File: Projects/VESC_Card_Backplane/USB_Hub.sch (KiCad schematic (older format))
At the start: 22 parts

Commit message: Added stuff to VESC_Card_Backplane
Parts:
- removed USB? (x3): USB-TYPA, USB-A-F-PTH, symbol USB-TYPA
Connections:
- net labels added: DM_1, DM_2, DM_3, DP_1, DP_2, DP_3
- wire segments 94 -> 87
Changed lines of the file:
@@
-	1    0    0    -1
-$EndComp
-$Comp
-L +5V #U$07
-U 1 1 57E6D8D3
-P 8450 6350
-F 0 "#U$07" H 8375 6450 60  0001 L BNN
-F 1 "+5V" H 8350 6500 60  0000 L BNN
-F 2 "" H 8450 6350 60  0001 C CNN
-F 3 "" H 8450 6350 60  0001 C CNN
-	1    8450 6350
 	1    0    0    -1
 $EndComp
@@
 GND
 Text GLabel 4650 6800 3    10   UnSpc ~ 0
-GND
-Text GLabel 6650 5550 3    10   UnSpc ~ 0
-GND
-Text GLabel 6650 6950 1    10   UnSpc ~ 0
-GND
-Text GLabel 7050 5850 3    10   UnSpc ~ 0
-GND
-Text GLabel 7450 6150 3    10   UnSpc ~ 0
 GND
 Text Label 4750 5850 0    10   ~ 0
@@
 Text Label 4600 4750 0    10   ~ 0
 VBUS
-Text Label 6950 5550 3    10   ~ 0
-VBUS
-Text Label 7750 6150 3    10   ~ 0
-VBUS
 Text Label 7350 5850 3    10   ~ 0
-VBUS
-Text Label 8450 6350 3    10   ~ 0
 VBUS
 $Comp
@@
 $EndComp
 $Comp
-L USB-TYPA USB?
-U 1 1 58632E73
-P 7600 5900
-F 0 "USB?" H 7600 6150 45  0000 C CNN
-F 1 "USB-TYPA" V 7700 5900 45  0000 C CNN
-F 2 "USB-A-F-PTH" H 7600 5600 20  0001 C CNN
-F 3 "" H 7600 5900 60  0000 C CNN
-	1    7600 5900
-	0    1    -1   0
-$EndComp
-$Comp
-L USB-TYPA USB?
-U 1 1 586331D9
-P 6800 5300
-F 0 "USB?" H 6800 5550 45  0000 C CNN
-F 1 "USB-TYPA" V 6900 5300 45  0000 C CNN
-F 2 "USB-A-F-PTH" H 6800 5000 20  0001 C CNN
-F 3 "" H 6800 5300 60  0000 C CNN
-	1    6800 5300
-	0    1    -1   0
-$EndComp
-$Comp
-L USB-TYPA USB?
-U 1 1 58633244
-P 7200 5600
-F 0 "USB?" H 7200 5850 45  0000 C CNN
-F 1 "USB-TYPA" V 7300 5600 45  0000 C CNN
-F 2 "USB-A-F-PTH" H 7200 5300 20  0001 C CNN
-F 3 "" H 7200 5600 60  0000 C CNN
-	1    7200 5600
-	0    1    -1   0
-$EndComp
-$Comp
 L XTAL_1 XL1
 U 1 1 57E6DDE7
@@
 	0    1    -1   0
 $EndComp
-$Comp
-L GND #GND?
-U 1 1 586383BE
-P 6650 6950
-F 0 "#GND?" H 6650 6950 45  0001 L BNN
-F 1 "GND" H 6600 6775 45  0000 L BNN
-F 2 "" H 6650 6950 60  0001 C CNN
-F 3 "" H 6650 6950 60  0001 C CNN
-	1    6650 6950
+Text HLabel 4850 7600 0    60   Input ~ 0
+DM_U
+Text HLabel 4850 7700 0    60   Input ~ 0
+DP_U
+Text Notes 4900 7850 0    60   ~ 0
+Upstream USB Connection
+$Comp
+L VDD #PWR?
+U 1 1 58718D88
+P 4850 5350
+F 0 "#PWR?" H 4850 5200 50  0001 C CNN
+F 1 "VDD" H 4850 5500 50  0000 C CNN
+F 2 "" H 4850 5350 50  0000 C CNN
+F 3 "" H 4850 5350 50  0000 C CNN
+	1    4850 5350
 	1    0    0    -1
 $EndComp
+Text HLabel 8050 6450 1    60   Input ~ 0
+DM_4
+Text HLabel 7950 6450 1    60   Input ~ 0
+DP_4
+Text HLabel 7650 6150 1    60   Input ~ 0
+DM_3
+Text HLabel 7550 6150 1    60   Input ~ 0
+DP_3
+Text HLabel 7250 5850 1    60   Input ~ 0
+DM_2
+Text HLabel 7150 5850 1    60   Input ~ 0
+DP_2
+Text HLabel 6850 5550 1    60   Input ~ 0
+DM_1
+Text HLabel 6750 5550 1    60   Input ~ 0
+DP_1
+$Comp
+L GND #PWR?
+U 1 1 5871A6C2
+P 2250 6775
+F 0 "#PWR?" H 2250 6525 50  0001 C CNN
+F 1 "GND" H 2250 6625 50  0000 C CNN
+F 2 "" H 2250 6775 50  0000 C CNN
+F 3 "" H 2250 6775 50  0000 C CNN
+	1    2250 6775
+	1    0    0    -1
+$EndComp
+$Comp
+L +5V #PWR?
+U 1 1 5871A6FC
+P 2175 5325
+F 0 "#PWR?" H 2175 5175 50  0001 C CNN
+F 1 "+5V" H 2175 5465 50  0000 C CNN
+F 2 "" H 2175 5325 50  0000 C CNN
+F 3 "" H 2175 5325 50  0000 C CNN
+	1    2175 5325
+	1    0    0    -1
+$EndComp
+Text HLabel 2250 6575 1    60   Input ~ 0
+GND
+Text HLabel 2175 5600 3    60   Input ~ 0
++5V
 Wire Wire Line
 	5300 5150 5250 5150
@@
 Wire Wire Line
 	4850 6350 5300 6350
-Wire Wire Line
-	5250 6350 5250 6250
 Wire Wire Line
 	4850 6350 4850 6450
@@
 Connection ~ 4650 6850
 Wire Wire Line
-	6650 5550 6650 6950
-Wire Wire Line
-	7050 5850 7050 6850
-Wire Wire Line
-	7450 6850 7450 6150
-Connection ~ 6650 6850
-Connection ~ 7050 6850
-Connection ~ 7450 6850
-Wire Wire Line
-	7650 5350 7650 5250
+	7650 5200 7650 5350
 Wire Wire Line
 	4700 5850 5300 5850
@@
 Connection ~ 4700 4750
 Wire Wire Line
-	6950 5550 6950 6750
-Wire Wire Line
-	7750 6750 7750 6150
-Wire Wire Line
-	6950 6750 8450 6750
-Wire Wire Line
-	7350 5850 7350 6750
-Wire Wire Line
-	8450 6750 8450 6350
-Connection ~ 7750 6750
-Connection ~ 7350 6750
-Text HLabel 4850 7600 0    60   Input ~ 0
-DM_U
-Text HLabel 4850 7700 0    60   Input ~ 0
-DP_U
-Text Notes 4900 7850 0    60   ~ 0
-Upstream USB Connection
-$Comp
-L VDD #PWR?
-U 1 1 58718D88
-P 4850 5350
-F 0 "#PWR?" H 4850 5200 50  0001 C CNN
-F 1 "VDD" H 4850 5500 50  0000 C CNN
-F 2 "" H 4850 5350 50  0000 C CNN
-F 3 "" H 4850 5350 50  0000 C CNN
-	1    4850 5350
-	1    0    0    -1
-$EndComp
-Text HLabel 8050 6450 1    60   Input ~ 0
-DM_4
-Text HLabel 7950 6450 1    60   Input ~ 0
-DP_4
-Wire Wire Line
-	6650 6850 7450 6850
+	5250 6350 5250 6250
+Wire Wire Line
+	2175 5325 2175 5600
+Wire Wire Line
+	2250 6575 2250 6775
 $EndSCHEMATC

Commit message: Updated subsheets and added CAN bus :)
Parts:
- added JP1: Jumper_NC_Small, symbol Jumper_NC_Small
- added U1: LP38693, symbol LP38693
- gave numbers to parts that had none: 1
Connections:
- net labels added: GNDD
- wire segments 87 -> 94
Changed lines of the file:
@@
 $Descr A3 16535 11693
 encoding utf-8
-Sheet 2 5
+Sheet 2 6
 Title "RH025.1.sch"
 Date "24 SEP 2016"
@@
 $EndComp
 $Comp
-L GND #GND03
+L GNDD #GND1
 U 1 1 57E6CBEF
 P 4550 6900
-F 0 "#GND03" H 4450 6900 60  0001 L BNN
-F 1 "GND" H 4475 6725 60  0000 L BNN
+F 0 "#GND1" H 4450 6900 60  0001 L BNN
+F 1 "GNDD" H 4475 6725 60  0000 L BNN
 F 2 "" H 4550 6900 60  0001 C CNN
 F 3 "" H 4550 6900 60  0001 C CNN
@@
 $EndComp
 $Comp
-L GND #GND04
+L GNDD #GND2
 U 1 1 57E6CC53
 P 7650 5350
-F 0 "#GND04" H 7550 5350 60  0001 L BNN
-F 1 "GND" H 7575 5175 60  0000 L BNN
+F 0 "#GND2" H 7550 5350 60  0001 L BNN
+F 1 "GNDD" H 7575 5175 60  0000 L BNN
 F 2 "" H 7650 5350 60  0001 C CNN
 F 3 "" H 7650 5350 60  0001 C CNN
@@
 $EndComp
 $Comp
-L +5V #U$05
+L +5V #U$2
 U 1 1 57E6D80B
 P 5250 4300
-F 0 "#U$05" H 5175 4400 60  0001 L BNN
+F 0 "#U$2" H 5175 4400 60  0001 L BNN
 F 1 "+5V" H 5150 4500 60  0000 L BNN
 F 2 "" H 5250 4300 60  0001 C CNN
@@
 VBUS
 $Comp
-L FE1.1S M?
+L FE1.1S M1
 U 1 1 5862FDC9
 P 5900 5550
-F 0 "M?" H 5500 6780 45  0000 L BNN
+F 0 "M1" H 5500 6780 45  0000 L BNN
 F 1 "FE1.1S" H 5900 5550 45  0001 L BNN
 F 2 "FE1.1S_SSOP-28" H 5930 5700 20  0001 C CNN
@@
 Upstream USB Connection
 $Comp
-L VDD #PWR?
+L VDD #PWR2
 U 1 1 58718D88
 P 4850 5350
-F 0 "#PWR?" H 4850 5200 50  0001 C CNN
+F 0 "#PWR2" H 4850 5200 50  0001 C CNN
 F 1 "VDD" H 4850 5500 50  0000 C CNN
 F 2 "" H 4850 5350 50  0000 C CNN
@@
 DP_1
 $Comp
-L GND #PWR?
+L GNDD #PWR1
 U 1 1 5871A6C2
-P 2250 6775
-F 0 "#PWR?" H 2250 6525 50  0001 C CNN
-F 1 "GND" H 2250 6625 50  0000 C CNN
-F 2 "" H 2250 6775 50  0000 C CNN
-F 3 "" H 2250 6775 50  0000 C CNN
-	1    2250 6775
-	1    0    0    -1
-$EndComp
-$Comp
-L +5V #PWR?
-U 1 1 5871A6FC
-P 2175 5325
-F 0 "#PWR?" H 2175 5175 50  0001 C CNN
-F 1 "+5V" H 2175 5465 50  0000 C CNN
-F 2 "" H 2175 5325 50  0000 C CNN
-F 3 "" H 2175 5325 50  0000 C CNN
-	1    2175 5325
-	1    0    0    -1
-$EndComp
-Text HLabel 2250 6575 1    60   Input ~ 0
-GND
-Text HLabel 2175 5600 3    60   Input ~ 0
+P 3350 6375
+F 0 "#PWR1" H 3350 6125 50  0001 C CNN
+F 1 "GNDD" H 3350 6225 50  0000 C CNN
+F 2 "" H 3350 6375 50  0000 C CNN
+F 3 "" H 3350 6375 50  0000 C CNN
+	1    3350 6375
+	1    0    0    -1
+$EndComp
+Text HLabel 3350 6175 1    60   Input ~ 0
+GND
+Text HLabel 3350 5600 3    60   Input ~ 0
 +5V
 Wire Wire Line
@@
 	5200 6550 5300 6550
 Wire Wire Line
-	4850 6750 4850 6850
-Wire Wire Line
-	4850 6850 4100 6850
+	4850 6850 4850 6750
+Wire Wire Line
+	4100 6850 4850 6850
 Wire Wire Line
 	4550 6850 4550 6900
@@
 	4100 5850 4400 5850
 Wire Wire Line
-	4100 6850 4100 4450
+	4100 4450 4100 6850
 Wire Wire Line
 	4100 4450 5300 4450
@@
 	5250 6350 5250 6250
 Wire Wire Line
-	2175 5325 2175 5600
-Wire Wire Line
-	2250 6575 2250 6775
+	3350 6175 3350 6375
+Wire Wire Line
+	3350 5600 3350 5350
+$Comp
+L +5V #U$1
+U 1 1 587820C5
+P 3350 5350
+F 0 "#U$1" H 3275 5450 60  0001 L BNN
+F 1 "+5V" H 3250 5550 60  0000 L BNN
+F 2 "" H 3350 5350 60  0001 C CNN
+F 3 "" H 3350 5350 60  0001 C CNN
+	1    3350 5350
+	1    0    0    -1
+$EndComp
+$Comp
+L LP38693 U1
+U 1 1 58783463
+P 10100 5400
+F 0 "U1" H 10250 5100 60  0000 C CNN
+F 1 "LP38693" H 10100 5700 60  0000 C CNN
+F 2 "" H 10100 5400 60  0001 C CNN
+F 3 "" H 10100 5400 60  0001 C CNN
+	1    10100 5400
+	1    0    0    -1
+$EndComp
+$Comp
+L VDD #PWR3
+U 1 1 587837CA
+P 10900 5350
+F 0 "#PWR3" H 10900 5200 50  0001 C CNN
+F 1 "VDD" H 10900 5500 50  0000 C CNN
+F 2 "" H 10900 5350 50  0000 C CNN
+F 3 "" H 10900 5350 50  0000 C CNN
+	1    10900 5350
+	1    0    0    -1
+$EndComp
+Wire Wire Line
+	10900 5350 10900 5400
+Wire Wire Line
+	10900 5400 10550 5400
+Wire Wire Line
+	9650 5400 9150 5400
+Wire Wire Line
+	9150 5400 9150 5350
+$Comp
+L +5V #U$3
+U 1 1 58783B06
+P 9150 5350
+F 0 "#U$3" H 9075 5450 60  0001 L BNN
+F 1 "+5V" H 9050 5550 60  0000 L BNN
+F 2 "" H 9150 5350 60  0001 C CNN
+F 3 "" H 9150 5350 60  0001 C CNN
+	1    9150 5350
+	1    0    0    -1
+$EndComp
+$Comp
+L GNDD #GND3
+U 1 1 58784370
+P 10100 5900
+F 0 "#GND3" H 10000 5900 60  0001 L BNN
+F 1 "GNDD" H 10025 5725 60  0000 L BNN
+F 2 "" H 10100 5900 60  0001 C CNN
+F 3 "" H 10100 5900 60  0001 C CNN
+	1    10100 5900
+	1    0    0    -1
+$EndComp
+Wire Wire Line
+	10100 5800 10100 5900
+$Comp
+L Jumper_NC_Small JP1
+U 1 1 5878491B
+P 9550 5300
+F 0 "JP1" H 9550 5380 50  0000 C CNN
+F 1 "Jumper_NC_Small" H 9560 5240 50  0001 C CNN
+F 2 "" H 9550 5300 50  0000 C CNN
+F 3 "" H 9550 5300 50  0000 C CNN
+	1    9550 5300
+	1    0    0    -1
+$EndComp
+Wire Wire Line
+	9450 5300 9350 5300
+Wire Wire Line
+	9350 5300 9350 5400
+Connection ~ 9350 5400
 $EndSCHEMATC

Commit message: Footprint assoc. for backplane
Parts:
- ACT1: renamed from ACT7; symbol LED_SMT -> LED
- JP1: footprint (none) -> USST-footprints:J_0603
- M1: footprint FE1.1S_SSOP-28 -> USST-footprints:FE1.1S_SSOP-28
- PORT1, PORT2, PORT3, PORT4: symbol LED_SMT -> LED
- U1: footprint (none) -> USST-footprints:SOT-223_5-pin
- XL1: footprint RH025.1:HC49UP -> USST-footprints:HC49UP_SMT_Crystal
- renumbered C4 to C1, C5 to C2, C6 to C3, C3 to C4, C2 to C5, C1 to C6, REXT7 to REXT1
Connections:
- net N$20: now also PORT1.1 (K), PORT3.2 (A); no longer PORT1.C, PORT3.A
- net N$22: now also ACT1.1 (K); no longer ACT1.C
- net N$25: now also ACT1.2 (A), PORT1.2 (A), PORT2.2 (A), PORT3.1 (K), PORT4.1 (K); no longer ACT1.A, PORT1.A, PORT2.A, PORT3.C, PORT4.C
- net N$6: now also PORT2.1 (K), PORT4.2 (A); no longer PORT2.C, PORT4.A
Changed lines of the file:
@@
 $EndDescr
 $Comp
-L LED_SMT ACT7
+L LED ACT1
 U 1 1 57E6C5AF
-P 7650 4700
-F 0 "ACT7" V 7750 4850 60  0000 L BNN
-F 1 "~" H 7640 4590 65  0001 L TNN
-F 2 "LEDs:LED_0805" H 7640 4490 65  0001 L TNN
-F 3 "" H 7650 4700 60  0001 C CNN
-	1    7650 4700
+P 7650 4650
+F 0 "ACT1" V 7750 4800 60  0000 L BNN
+F 1 "~" H 7640 4540 65  0001 L TNN
+F 2 "LEDs:LED_0805" H 7640 4440 65  0001 L TNN
+F 3 "" H 7650 4650 60  0001 C CNN
+	1    7650 4650
 	0    1    -1   0
 $EndComp
 $Comp
-L C C1
+L C C6
 U 1 1 57E6C677
 P 4850 6600
-F 0 "C1" V 4835 6410 60  0000 L BNN
+F 0 "C6" V 4835 6410 60  0000 L BNN
 F 1 "0.1uF" V 4925 6665 60  0000 L BNN
 F 2 "Capacitors_SMD:C_0805" H 4840 6390 65  0001 L TNN
@@
 $EndComp
 $Comp
-L C C2
+L C C5
 U 1 1 57E6C73F
 P 4650 6600
-F 0 "C2" V 4635 6410 60  0000 L BNN
+F 0 "C5" V 4635 6410 60  0000 L BNN
 F 1 "10uF" V 4725 6665 60  0000 L BNN
 F 2 "Capacitors_SMD:C_0805" H 4640 6390 65  0001 L TNN
@@
 $EndComp
 $Comp
-L C C3
+L C C4
 U 1 1 57E6C807
 P 4450 6600
-F 0 "C3" V 4435 6410 60  0000 L BNN
+F 0 "C4" V 4435 6410 60  0000 L BNN
 F 1 "0.1uF" V 4525 6665 60  0000 L BNN
 F 2 "Capacitors_SMD:C_0805" H 4440 6390 65  0001 L TNN
@@
 $EndComp
 $Comp
-L C C4
+L C C1
 U 1 1 57E6C8CF
 P 4250 6600
-F 0 "C4" V 4235 6410 60  0000 L BNN
+F 0 "C1" V 4235 6410 60  0000 L BNN
 F 1 "10uF" V 4325 6665 60  0000 L BNN
 F 2 "Capacitors_SMD:C_0805" H 4240 6390 65  0001 L TNN
@@
 $EndComp
 $Comp
-L GNDD #GND1
+L GNDD #GND01
 U 1 1 57E6CBEF
 P 4550 6900
-F 0 "#GND1" H 4450 6900 60  0001 L BNN
+F 0 "#GND01" H 4450 6900 60  0001 L BNN
 F 1 "GNDD" H 4475 6725 60  0000 L BNN
 F 2 "" H 4550 6900 60  0001 C CNN
@@
 $EndComp
 $Comp
-L GNDD #GND2
+L GNDD #GND02
 U 1 1 57E6CC53
 P 7650 5350
-F 0 "#GND2" H 7550 5350 60  0001 L BNN
+F 0 "#GND02" H 7550 5350 60  0001 L BNN
 F 1 "GNDD" H 7575 5175 60  0000 L BNN
 F 2 "" H 7650 5350 60  0001 C CNN
@@
 $EndComp
 $Comp
-L LED_SMT PORT1
+L LED PORT1
 U 1 1 57E6CFD7
-P 7250 4550
-F 0 "PORT1" V 7226 4150 60  0000 L BNN
-F 1 "~" V 7325 4250 60  0000 L BNN
-F 2 "LEDs:LED_0805" H 7240 4340 65  0001 L TNN
-F 3 "" H 7250 4550 60  0001 C CNN
-	1    7250 4550
-	1    0    0    -1
-$EndComp
-$Comp
-L LED_SMT PORT2
+P 7300 4550
+F 0 "PORT1" V 7276 4150 60  0000 L BNN
+F 1 "~" V 7375 4250 60  0000 L BNN
+F 2 "LEDs:LED_0805" H 7290 4340 65  0001 L TNN
+F 3 "" H 7300 4550 60  0001 C CNN
+	1    7300 4550
+	1    0    0    -1
+$EndComp
+$Comp
+L LED PORT2
 U 1 1 57E6D09F
-P 7250 4950
-F 0 "PORT2" V 7201 4550 60  0000 L BNN
-F 1 "~" V 7325 4650 60  0000 L BNN
-F 2 "LEDs:LED_0805" H 7240 4740 65  0001 L TNN
-F 3 "" H 7250 4950 60  0001 C CNN
-	1    7250 4950
-	1    0    0    -1
-$EndComp
-$Comp
-L LED_SMT PORT3
+P 7300 4950
+F 0 "PORT2" V 7251 4550 60  0000 L BNN
+F 1 "~" V 7375 4650 60  0000 L BNN
+F 2 "LEDs:LED_0805" H 7290 4740 65  0001 L TNN
+F 3 "" H 7300 4950 60  0001 C CNN
+	1    7300 4950
+	1    0    0    -1
+$EndComp
+$Comp
+L LED PORT3
 U 1 1 57E6D167
-P 7350 4650
-F 0 "PORT3" V 7325 4675 60  0000 L BNN
-F 1 "~" H 7340 4540 65  0001 L TNN
-F 2 "LEDs:LED_0805" H 7340 4440 65  0001 L TNN
-F 3 "" H 7350 4650 60  0001 C CNN
-	1    7350 4650
+P 7300 4650
+F 0 "PORT3" V 7275 4675 60  0000 L BNN
+F 1 "~" H 7290 4540 65  0001 L TNN
+F 2 "LEDs:LED_0805" H 7290 4440 65  0001 L TNN
+F 3 "" H 7300 4650 60  0001 C CNN
+	1    7300 4650
 	-1   0    0    1
 $EndComp
 $Comp
-L LED_SMT PORT4
+L LED PORT4
 U 1 1 57E6D22F
-P 7350 5050
-F 0 "PORT4" V 7325 5075 60  0000 L BNN
-F 1 "~" H 7340 4940 65  0001 L TNN
-F 2 "LEDs:LED_0805" H 7340 4840 65  0001 L TNN
-F 3 "" H 7350 5050 60  0001 C CNN
-	1    7350 5050
+P 7300 5050
+F 0 "PORT4" V 7275 5075 60  0000 L BNN
+F 1 "~" H 7290 4940 65  0001 L TNN
+F 2 "LEDs:LED_0805" H 7290 4840 65  0001 L TNN
+F 3 "" H 7300 5050 60  0001 C CNN
+	1    7300 5050
 	-1   0    0    1
 $EndComp
@@
 $EndComp
 $Comp
-L R REXT7
+L R REXT1
 U 1 1 57E6D6DF
 P 4550 5850
-F 0 "REXT7" V 4475 5725 60  0000 L BNN
+F 0 "REXT1" V 4475 5725 60  0000 L BNN
 F 1 "2.7K" V 4675 5750 60  0000 L BNN
 F 2 "Resistors_SMD:R_0805" H 4540 5640 65  0001 L TNN
@@
 $EndComp
 $Comp
-L +5V #U$2
+L +5V #U$03
 U 1 1 57E6D80B
 P 5250 4300
-F 0 "#U$2" H 5175 4400 60  0001 L BNN
+F 0 "#U$03" H 5175 4400 60  0001 L BNN
 F 1 "+5V" H 5150 4500 60  0000 L BNN
 F 2 "" H 5250 4300 60  0001 C CNN
@@
 F 0 "M1" H 5500 6780 45  0000 L BNN
 F 1 "FE1.1S" H 5900 5550 45  0001 L BNN
-F 2 "FE1.1S_SSOP-28" H 5930 5700 20  0001 C CNN
+F 2 "USST-footprints:FE1.1S_SSOP-28" H 5930 5700 20  0001 C CNN
 F 3 "" H 5900 5550 60  0001 C CNN
 	1    5900 5550
@@
 $EndComp
 $Comp
-L C C5
+L C C2
 U 1 1 57E6C997
 P 4400 4550
-F 0 "C5" V 4386 4360 60  0000 L BNN
+F 0 "C2" V 4386 4360 60  0000 L BNN
 F 1 "10uF" V 4474 4615 60  0000 L BNN
 F 2 "Capacitors_SMD:C_0805" H 4390 4340 65  0001 L TNN
@@
 $EndComp
 $Comp
-L C C6
+L C C3
 U 1 1 57E6CA5F
 P 4400 4750
-F 0 "C6" V 4386 4560 60  0000 L BNN
+F 0 "C3" V 4386 4560 60  0000 L BNN
 F 1 "0.1uF" V 4474 4815 60  0000 L BNN
 F 2 "Capacitors_SMD:C_0805" H 4390 4540 65  0001 L TNN
@@
 F 0 "XL1" H 5050 4550 60  0000 L BNN
 F 1 "12MHz" H 4950 4650 60  0000 L BNN
-F 2 "RH025.1:HC49UP" H 5090 4590 65  0001 L TNN
+F 2 "USST-footprints:HC49UP_SMT_Crystal" H 5090 4590 65  0001 L TNN
 F 3 "" H 5100 4800 60  0001 C CNN
 	1    5100 4800
@@
 Upstream USB Connection
 $Comp
-L VDD #PWR2
+L VDD #PWR04
 U 1 1 58718D88
 P 4850 5350
-F 0 "#PWR2" H 4850 5200 50  0001 C CNN
+F 0 "#PWR04" H 4850 5200 50  0001 C CNN
 F 1 "VDD" H 4850 5500 50  0000 C CNN
 F 2 "" H 4850 5350 50  0000 C CNN
@@
 DP_1
 $Comp
-L GNDD #PWR1
+L GNDD #PWR05
 U 1 1 5871A6C2
 P 3350 6375
-F 0 "#PWR1" H 3350 6125 50  0001 C CNN
+F 0 "#PWR05" H 3350 6125 50  0001 C CNN
 F 1 "GNDD" H 3350 6225 50  0000 C CNN
 F 2 "" H 3350 6375 50  0000 C CNN
@@
 	3350 5600 3350 5350
 $Comp
-L +5V #U$1
+L +5V #U$06
 U 1 1 587820C5
 P 3350 5350
-F 0 "#U$1" H 3275 5450 60  0001 L BNN
+F 0 "#U$06" H 3275 5450 60  0001 L BNN
 F 1 "+5V" H 3250 5550 60  0000 L BNN
 F 2 "" H 3350 5350 60  0001 C CNN
@@
 F 0 "U1" H 10250 5100 60  0000 C CNN
 F 1 "LP38693" H 10100 5700 60  0000 C CNN
-F 2 "" H 10100 5400 60  0001 C CNN
+F 2 "USST-footprints:SOT-223_5-pin" H 10100 5400 60  0001 C CNN
 F 3 "" H 10100 5400 60  0001 C CNN
 	1    10100 5400
@@
 $EndComp
 $Comp
-L VDD #PWR3
+L VDD #PWR07
 U 1 1 587837CA
 P 10900 5350
-F 0 "#PWR3" H 10900 5200 50  0001 C CNN
+F 0 "#PWR07" H 10900 5200 50  0001 C CNN
 F 1 "VDD" H 10900 5500 50  0000 C CNN
 F 2 "" H 10900 5350 50  0000 C CNN
@@
 	9150 5400 9150 5350
 $Comp
-L +5V #U$3
+L +5V #U$08
 U 1 1 58783B06
 P 9150 5350
-F 0 "#U$3" H 9075 5450 60  0001 L BNN
+F 0 "#U$08" H 9075 5450 60  0001 L BNN
 F 1 "+5V" H 9050 5550 60  0000 L BNN
 F 2 "" H 9150 5350 60  0001 C CNN
@@
 $EndComp
 $Comp
-L GNDD #GND3
+L GNDD #GND09
 U 1 1 58784370
 P 10100 5900
-F 0 "#GND3" H 10000 5900 60  0001 L BNN
+F 0 "#GND09" H 10000 5900 60  0001 L BNN
 F 1 "GNDD" H 10025 5725 60  0000 L BNN
 F 2 "" H 10100 5900 60  0001 C CNN
@@
 F 0 "JP1" H 9550 5380 50  0000 C CNN
 F 1 "Jumper_NC_Small" H 9560 5240 50  0001 C CNN
-F 2 "" H 9550 5300 50  0000 C CNN
+F 2 "USST-footprints:J_0603" H 9550 5300 50  0001 C CNN
 F 3 "" H 9550 5300 50  0000 C CNN
 	1    9550 5300

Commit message: Comleted VESC Backplane
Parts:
- removed JP1: Jumper_NC_Small, USST-footprints:J_0603, symbol Jumper_NC_Small
- removed U1: LP38693, USST-footprints:SOT-223_5-pin, symbol LP38693
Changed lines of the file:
@@
 Text Label 5100 5000 3    10   ~ 0
 N$9
-Text Label 6500 5650 0    10   ~ 0
-N$11
-Text Label 6750 5550 3    10   ~ 0
-N$11
-Text Label 6500 5750 0    10   ~ 0
-N$12
-Text Label 6850 5550 3    10   ~ 0
-N$12
 Text Label 4700 5350 3    10   ~ 0
 N$13
@@
 Text Label 4600 5550 0    10   ~ 0
 N$13
-Text Label 6500 5950 0    10   ~ 0
-N$14
-Text Label 7150 5850 3    10   ~ 0
-N$14
-Text Label 6500 6050 0    10   ~ 0
-N$15
-Text Label 7250 5850 3    10   ~ 0
-N$15
-Text Label 7550 6150 3    10   ~ 0
-N$16
-Text Label 6500 6250 0    10   ~ 0
-N$16
-Text Label 6500 6350 0    10   ~ 0
-N$17
-Text Label 7650 6150 3    10   ~ 0
-N$17
-Text Label 6500 6550 0    10   ~ 0
-N$18
-Text Label 6500 6650 0    10   ~ 0
-N$19
 Text Label 7050 4600 0    10   ~ 0
 N$20
@@
 Text Label 4600 4750 0    10   ~ 0
 VBUS
-Text Label 7350 5850 3    10   ~ 0
-VBUS
 $Comp
 L FE1.1S M1
@@
 	1    0    0    -1
 $EndComp
-$Comp
-L LP38693 U1
-U 1 1 58783463
-P 10100 5400
-F 0 "U1" H 10250 5100 60  0000 C CNN
-F 1 "LP38693" H 10100 5700 60  0000 C CNN
-F 2 "USST-footprints:SOT-223_5-pin" H 10100 5400 60  0001 C CNN
-F 3 "" H 10100 5400 60  0001 C CNN
-	1    10100 5400
-	1    0    0    -1
-$EndComp
-$Comp
-L VDD #PWR07
-U 1 1 587837CA
-P 10900 5350
-F 0 "#PWR07" H 10900 5200 50  0001 C CNN
-F 1 "VDD" H 10900 5500 50  0000 C CNN
-F 2 "" H 10900 5350 50  0000 C CNN
-F 3 "" H 10900 5350 50  0000 C CNN
-	1    10900 5350
-	1    0    0    -1
-$EndComp
-Wire Wire Line
-	10900 5350 10900 5400
-Wire Wire Line
-	10900 5400 10550 5400
-Wire Wire Line
-	9650 5400 9150 5400
-Wire Wire Line
-	9150 5400 9150 5350
-$Comp
-L +5V #U$08
-U 1 1 58783B06
-P 9150 5350
-F 0 "#U$08" H 9075 5450 60  0001 L BNN
-F 1 "+5V" H 9050 5550 60  0000 L BNN
-F 2 "" H 9150 5350 60  0001 C CNN
-F 3 "" H 9150 5350 60  0001 C CNN
-	1    9150 5350
-	1    0    0    -1
-$EndComp
-$Comp
-L GNDD #GND09
-U 1 1 58784370
-P 10100 5900
-F 0 "#GND09" H 10000 5900 60  0001 L BNN
-F 1 "GNDD" H 10025 5725 60  0000 L BNN
-F 2 "" H 10100 5900 60  0001 C CNN
-F 3 "" H 10100 5900 60  0001 C CNN
-	1    10100 5900
-	1    0    0    -1
-$EndComp
-Wire Wire Line
-	10100 5800 10100 5900
-$Comp
-L Jumper_NC_Small JP1
-U 1 1 5878491B
-P 9550 5300
-F 0 "JP1" H 9550 5380 50  0000 C CNN
-F 1 "Jumper_NC_Small" H 9560 5240 50  0001 C CNN
-F 2 "USST-footprints:J_0603" H 9550 5300 50  0001 C CNN
-F 3 "" H 9550 5300 50  0000 C CNN
-	1    9550 5300
-	1    0    0    -1
-$EndComp
-Wire Wire Line
-	9450 5300 9350 5300
-Wire Wire Line
-	9350 5300 9350 5400
-Connection ~ 9350 5400
 $EndSCHEMATC

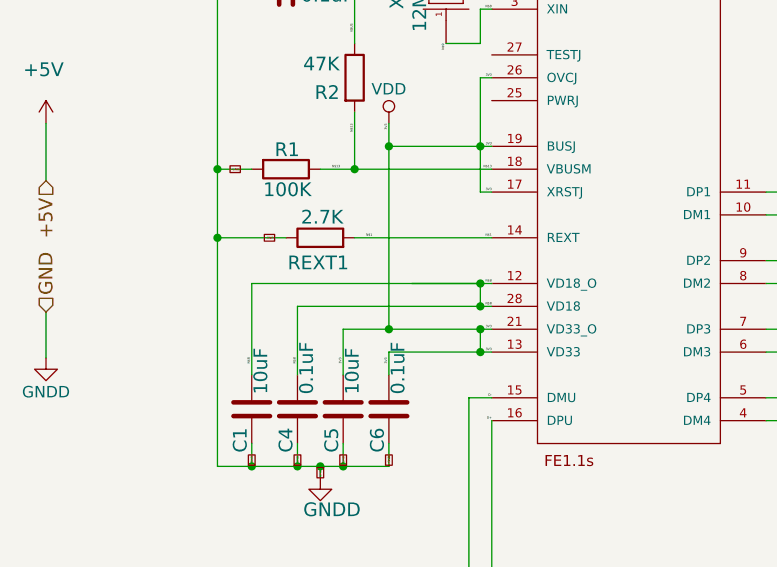
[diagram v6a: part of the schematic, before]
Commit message: Refactoring Compute Module project for 2017 USST KiCad library format
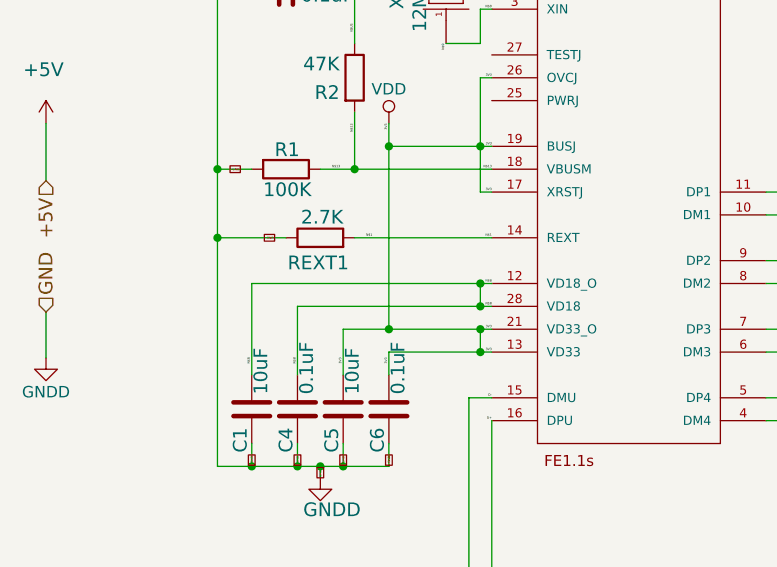
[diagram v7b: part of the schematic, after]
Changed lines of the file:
@@
 	5250 4750 5300 4750
-Wire Wire Line
-	4950 6050 5300 6050
 Wire Wire Line
 	4450 6150 5300 6150
@@
 	4450 6150 4450 6450
 Wire Wire Line
-	5250 6050 4250 6050
+	4250 6050 5300 6050
 Wire Wire Line
 	4250 6050 4250 6450
